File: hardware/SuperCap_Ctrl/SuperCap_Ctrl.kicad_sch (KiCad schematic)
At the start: 87 parts, among them J1 Conn_01x02, J2 Conn_01x04, J3 Conn_01x32_MountingPin, J4 Conn_01x03, Q1 Si2308, Q3 Si2308, Q4 Si2308, Q5 Si2308, Q6 Si2308, U1 STM32G474VCTx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

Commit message: wip: before subtree sync
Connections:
- net GND: now also Q1.2 (D); no longer Q1.3 (D)
- net at R10.2: now also Q6.2 (D); no longer Q6.3 (D)
- net at Buzzer1.N, D1.2 (A): now also Q1.3 (S); no longer Q1.2 (S)
- net at R7.2: now also Q3.2 (D); no longer Q3.3 (D)
- net at Q4.2 (D): now also R8.2; no longer D6.3 (K1)
- net at Q4.3 (S): now also D6.3 (K1); no longer R8.2
- net at R9.2: now also Q5.2 (D); no longer Q5.3 (D)
- net at D6.4 (K2): now also Q3.3 (S); no longer Q3.2 (S)
- net at D7.3 (K1): now also Q6.3 (S); no longer Q6.2 (S)
- net at D7.4 (K2): now also Q5.3 (S); no longer Q5.2 (S)
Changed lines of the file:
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@@
 	)
 	(symbol
+		(lib_name "Si2319CDS_3")
 		(lib_id "Transistor_FET:Si2319CDS")
 		(at 267.97 22.86 180)
@@
 	)
 	(symbol
+		(lib_name "Si2319CDS_4")
 		(lib_id "Transistor_FET:Si2319CDS")
 		(at 267.97 45.72 180)
@@
 	)
 	(symbol
+		(lib_name "Si2319CDS_2")
 		(lib_id "Transistor_FET:Si2319CDS")
 		(at 247.65 27.94 180)
@@
 	)
 	(symbol
+		(lib_name "Si2319CDS_1")
 		(lib_id "Transistor_FET:Si2319CDS")
 		(at 247.65 50.8 180)

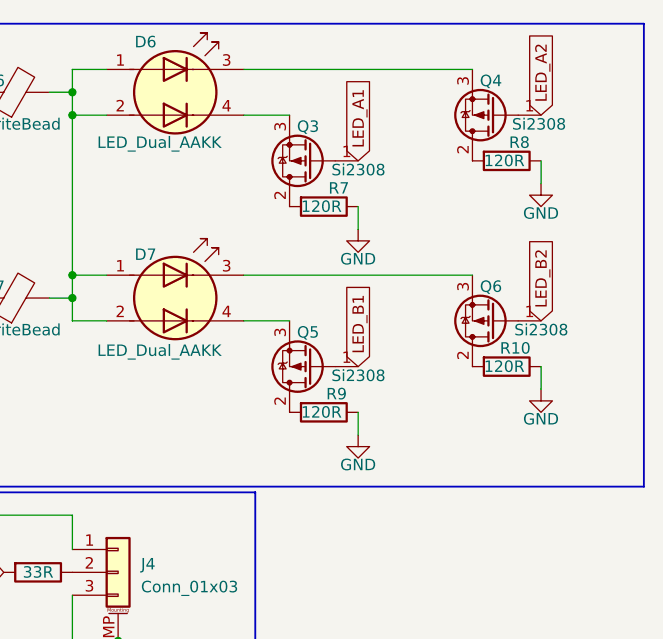
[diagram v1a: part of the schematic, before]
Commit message: 修改LED电路
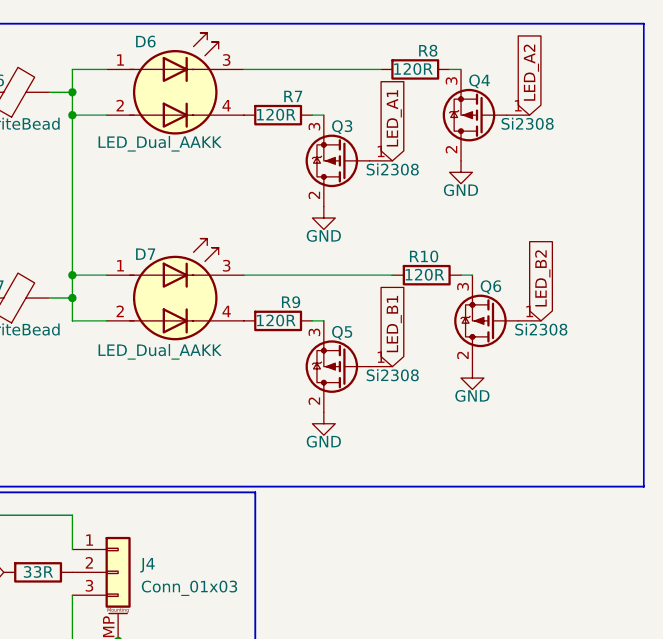
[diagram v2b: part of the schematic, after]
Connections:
- net GND: now also Q3.2 (D), Q4.2 (D), Q5.2 (D), Q6.2 (D); no longer R10.1, R7.1, R8.1, R9.1
- net at R10.2: now also D7.3 (K1); no longer Q6.2 (D)
- net at R7.2: now also D6.4 (K2); no longer Q3.2 (D)
- net at R8.2: now also D6.3 (K1); no longer Q4.2 (D)
- net at Q4.3 (S): now also R8.1; no longer D6.3 (K1)
- net at R9.2: now also D7.4 (K2); no longer Q5.2 (D)
- net at Q3.3 (S): now also R7.1; no longer D6.4 (K2)
- net at Q6.3 (S): now also R10.1; no longer D7.3 (K1)
- net at Q5.3 (S): now also R9.1; no longer D7.4 (K2)
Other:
- moved on the sheet: Q3, Q4, Q5, R10, R7, R8, R9
